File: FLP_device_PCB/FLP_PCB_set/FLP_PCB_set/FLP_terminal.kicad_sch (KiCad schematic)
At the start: 0 parts

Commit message: FLP_set add
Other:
- added sheet BOOT_Mode (BOOT_Mode.kicad_sch)
- added sheet Bat (Bat.kicad_sch)
- added sheet GPS (GPS.kicad_sch)
- added sheet LoRa (LoRa.kicad_sch)
- added sheet USB_to_UART (USB_to_UART.kicad_sch)
- added sheet Voltage_convert (5v_to_3.3V.kicad_sch)
- sheet STM32 ports: added 3.3V_in, BOOT0, BOOT1, DIO0(IRQ), GPS_Reset, GPS_Rx, GPS_TX, MISO, MOSI, NSS(CS), RESET, RX, SCK, TX, VBAT; removed none
- sheet UART_USB ports: added 5V_USB; removed none

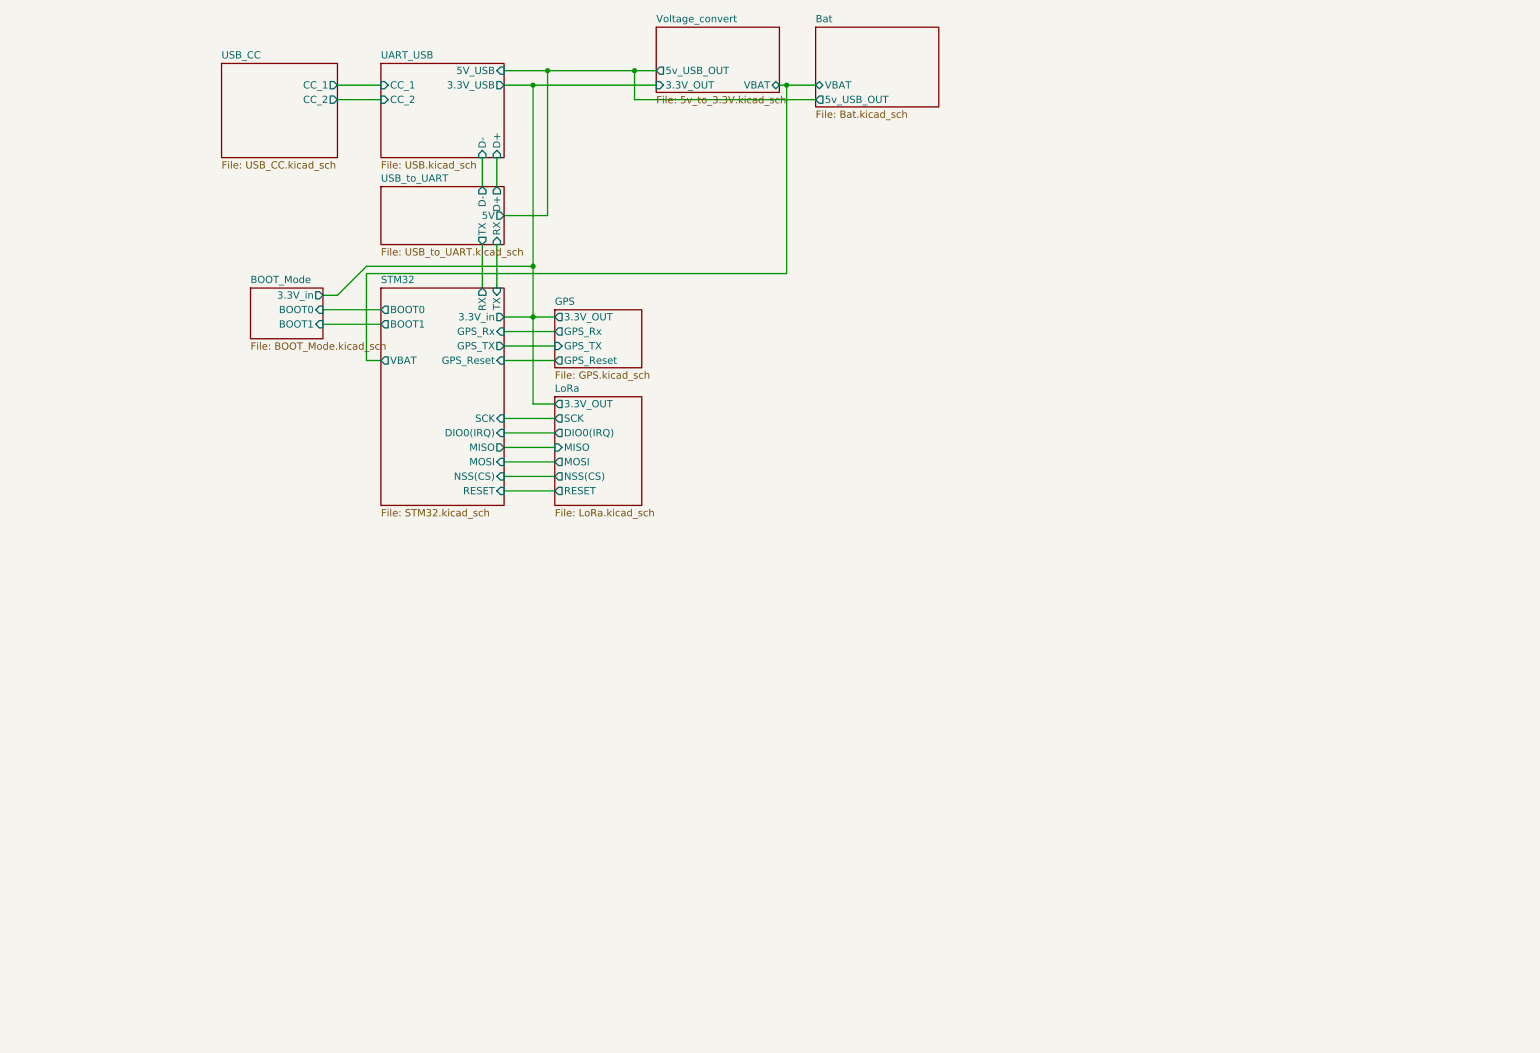
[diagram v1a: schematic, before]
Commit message: PCB fixing end adding description pdf
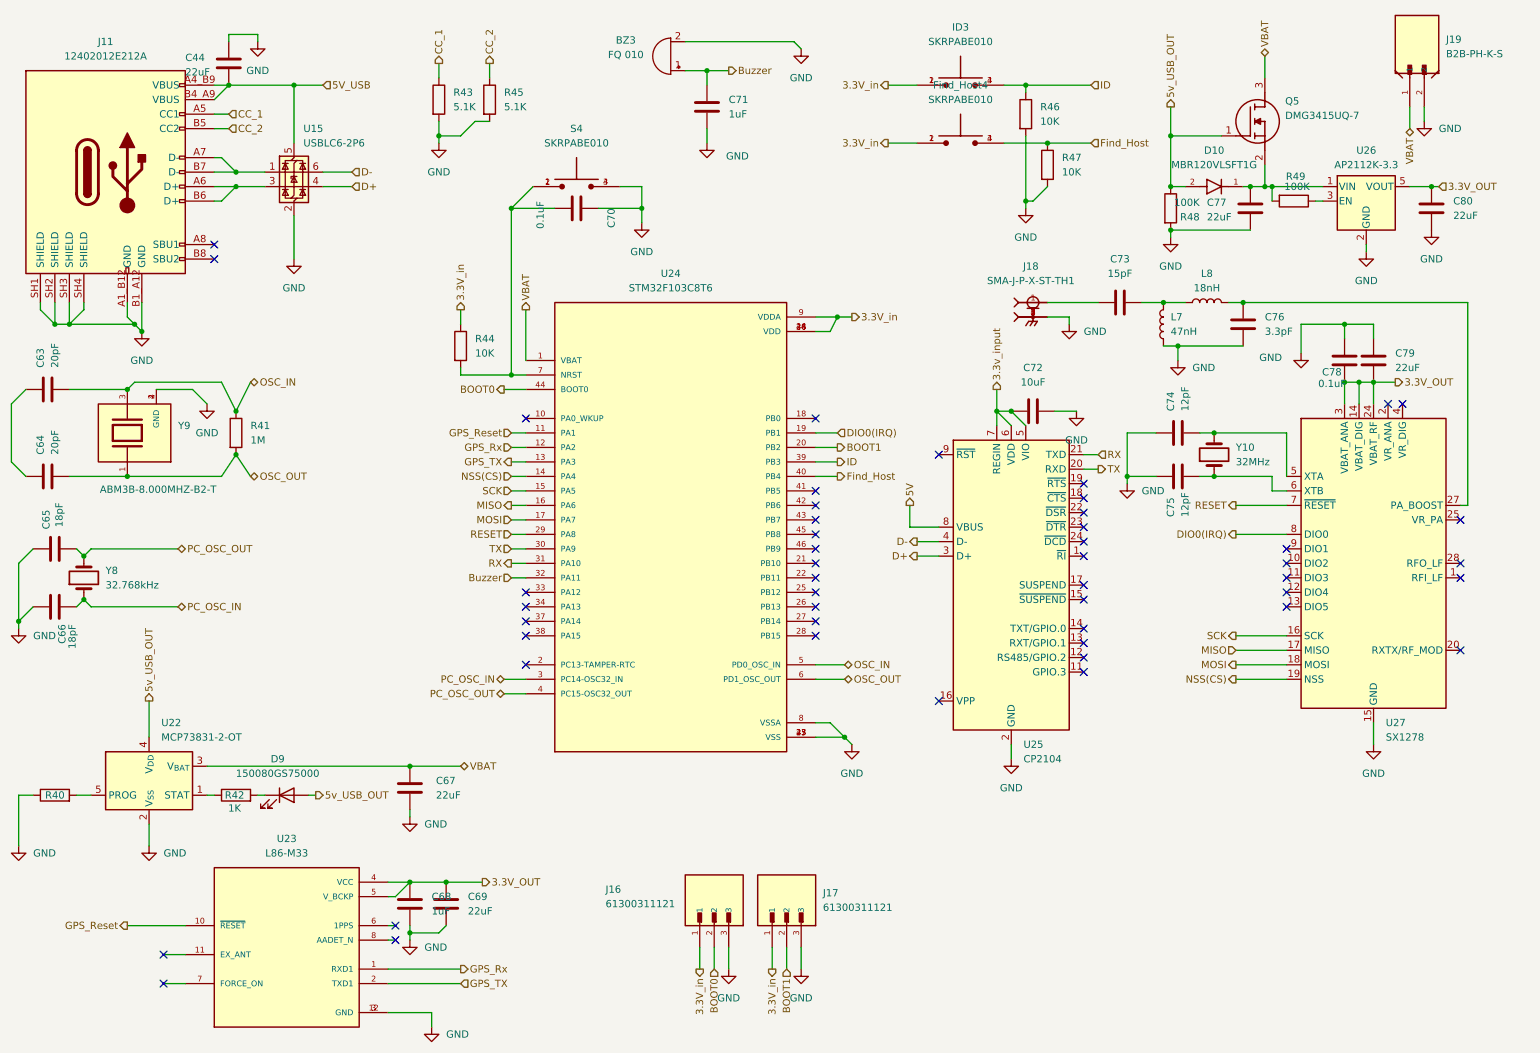
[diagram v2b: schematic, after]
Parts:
- added BZ3: FQ 010, Buzzer_Beeper:Buzzer_12x9.5RM7.6, symbol Device:Buzzer
- added C44, C67, C69, C77, C79, C80: 22uF, Capacitor_SMD:C_0805_2012Metric, symbol Device:C
- added C63, C64: 20pF, Capacitor_SMD:C_0402_1005Metric, symbol Device:C
- added C65, C66: 18pF, Capacitor_SMD:C_0603_1608Metric, symbol Device:C
- added C68, C71: 1uF, Capacitor_SMD:C_0603_1608Metric, symbol Device:C
- added C70, C78: 0.1uF, Capacitor_SMD:C_0603_1608Metric, symbol Device:C
- added C72: 10uF, Capacitor_SMD:C_0805_2012Metric, symbol Device:C
- added C73: 15pF, Capacitor_SMD:C_0402_1005Metric, symbol Device:C
- added C74, C75: 12pF, Capacitor_SMD:C_0402_1005Metric, symbol Device:C
- added C76: 3.3pF, Capacitor_SMD:C_0402_1005Metric, symbol Device:C
- added D10: MBR120VLSFT1G, MBR120VLSFT1G:DIOM3616X98N, symbol MBR120VLSFT1G:MBR120VLSFT1G
- added D9: 150080GS75000, LED_SMD:LED_0805_2012Metric, symbol Device:LED
- added Find_Host4, ID3, S4: SKRPABE010, Diode_SMD:SW_SKRPABE010, symbol SKRPABE010:SKRPABE010
- added J11: 12402012E212A, 12402012E212A:AMPHENOL_12402012E212A, symbol Connector:USB_C_Receptacle_USB2.0_16P
- added J16, J17: 61300311121, 61300311121:WURTH_61300311121, symbol 61300311121:61300311121
- added J18: SMA-J-P-X-ST-TH1, SMA-J-P-X-ST-TH1:SAMTEC_SMA-J-P-X-ST-TH1, symbol SMA-J-P-X-ST-TH1:SMA-J-P-X-ST-TH1
- added J19: B2B-PH-K-S, B2B_PH_K_S:JST_B2B-PH-K-S, symbol B2B-PH-K-S:B2B-PH-K-S
- added L7: 47nH, Inductor_SMD:L_0402_1005Metric, symbol Device:L
- added L8: 18nH, Inductor_SMD:L_0402_1005Metric, symbol Device:L
- added Q5: DMG3415UQ-7, symbol DMG3415UQ-7:DMG3415UQ-7
- added R40: 2K, Resistor_SMD:R_0402_1005Metric, symbol Device:R
- added R41: 1M, Resistor_SMD:R_0603_1608Metric, symbol Device:R
- added R42: 1K, Resistor_SMD:R_0603_1608Metric, symbol Device:R
- added R43, R45: 5.1K, Resistor_SMD:R_0603_1608Metric, symbol Device:R
- added R44, R46, R47: 10K, Resistor_SMD:R_0603_1608Metric, symbol Device:R
- added R48, R49: 100K, Resistor_SMD:R_0603_1608Metric, symbol Device:R
- added U15: USBLC6-2P6, Package_TO_SOT_SMD:SOT-666, symbol Power_Protection:USBLC6-2P6
- added U22: MCP73831-2-OT, Package_TO_SOT_SMD:SOT-23-5, symbol Battery_Management:MCP73831-2-OT
- added U23: L86-M33, L86-M33:XCVR_L86-M33, symbol L86-M33:L86-M33
- added U24: STM32F103C8T6, STM32F103C8T6:QFP50P900X900X160-48N, symbol STM32F103C8T6:STM32F103C8T6
- added U25: CP2104, Package_DFN_QFN:QFN-24-1EP_4x4mm_P0.5mm_EP2.6x2.6mm, symbol Interface_USB:CP2104
- added U26: AP2112K-3.3, Package_TO_SOT_SMD:SOT-23-5, symbol Regulator_Linear:AP2112K-3.3
- added U27: SX1278, Package_DFN_QFN:QFN-28-1EP_6x6mm_P0.65mm_EP4.8x4.8mm, symbol RF:SX1278
- added Y10: 32MHz, Crystal:Crystal_SMD_2016-4Pin_2.0x1.6mm, symbol Device:Crystal
- added Y8: 32.768kHz, Crystal:Crystal_SMD_3215-2Pin_3.2x1.5mm, symbol Device:Crystal
- added Y9: ABM3B-8.000MHZ-B2-T, ABM3B-8.000MHZ-B2-T:XTAL_ABM3B-8.000MHZ-B2-T, symbol ABM3B-8.000MHZ-B2-T:ABM3B-8.000MHZ-B2-T
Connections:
- new net: R40.2, U22.5 (PROG)
- new net: J11.A6 (D+), J11.B6 (D+), U15.3 (I/O2)
- new net: J11.A7 (D-), J11.B7 (D-), U15.1 (I/O1)
- new net: R42.1, U22.1 (STAT)
- new net: C70.2, R44.2, S4.1, S4.2, U24.7 (NRST)
- new net: C63.1, C64.1
- new net: D9.1 (K), R42.2
- new net: C77.1, D10.1, Q5.2 (S), R49.2, U26.1 (VIN)
- new net: R49.1, U26.3 (EN)
- new net: C73.2, J18.1
- new net: C74.2, U27.5 (XTA), Y10.2
- new net: C75.2, U27.6 (XTB), Y10.1
- new net: C76.1, L8.2, U27.27 (PA_BOOST)
- new net: C73.1, L7.2, L8.1
- new net 3.3V_OUT: C68.1, C69.1, C78.1, C79.2, C80.1, U23.4 (VCC), U23.5 (V_BCKP), U26.5 (VOUT), U27.14 (VBAT_DIG), U27.24 (VBAT_RF), U27.3 (VBAT_ANA)
- new net 3.3V_in: Find_Host4.1, Find_Host4.2, ID3.1, ID3.2, J16.1, J17.1, R44.1, U24.24 (VDD), U24.36 (VDD), U24.48 (VDD), U24.9 (VDDA)
- new net 3.3v_input: C72.1, U25.5 (VIO), U25.6 (VDD), U25.7 (REGIN)
- new net 5V: U25.8 (VBUS)
- new net 5V_USB: C44.2, J11.A4_B9 (VBUS), J11.A9 (VBUS), J11.B4 (VBUS), J11.B4_A9 (VBUS), J11.B9 (VBUS), U15.5 (VBUS)
- new net 5v_USB_OUT: D10.2, D9.2 (A), Q5.1 (G), R48.1, U22.4 (V_{DD})
- new net BOOT0: J16.2, U24.44 (BOOT0)
- new net BOOT1: J17.2, U24.20 (PB2)
- new net Buzzer: BZ3.1 (+), C71.1, U24.32 (PA11)
- new net CC_1: J11.A5 (CC1), R43.1
- new net CC_2: J11.B5 (CC2), R45.1
- new net D+: U15.4 (I/O2), U25.3 (D+)
- new net D-: U15.6 (I/O1), U25.4 (D-)
- new net DIO0(IRQ): U24.19 (PB1), U27.8 (DIO0)
- new net Find_Host: Find_Host4.3, Find_Host4.4, R47.1, U24.40 (PB4)
- new net GND: BZ3.2 (-), C44.1, C65.2, C66.2, C67.2, C68.2, C69.2, C70.1, C71.2, C72.2, C74.1, C75.1, C76.2, C77.2, C78.2, C79.1, C80.2, J11.A12 (GND), J11.A1_B12 (GND), J11.B1 (GND), J11.B12 (GND), J11.B1_A12 (GND), J11.SH1 (SHIELD), J11.SH2 (SHIELD), J11.SH3 (SHIELD), J11.SH4 (SHIELD), J16.3, J17.3, J18.2, J18.3, J18.4, J18.5, J19.2, L7.1, R40.1, R43.2, R45.2, R46.2, R47.2, R48.2, S4.3, S4.4, U15.2 (GND), U22.2 (V_{SS}), U23.12 (GND), U23.3 (GND), U24.23 (VSS), U24.35 (VSS), U24.47 (VSS), U24.8 (VSSA), U25.2 (GND), U25.25 (GND), U26.2 (GND), U27.15 (GND), U27.21 (GND), U27.22 (GND), U27.23 (GND), U27.26 (GND), U27.29 (GND), Y9.2 (GND), Y9.4 (GND)
- new net GPS_Reset: U23.10 (~{RESET}), U24.11 (PA1)
- new net GPS_Rx: U23.1 (RXD1), U24.12 (PA2)
- new net GPS_TX: U23.2 (TXD1), U24.13 (PA3)
- new net ID: ID3.3, ID3.4, R46.1, U24.39 (PB3)
- new net MISO: U24.16 (PA6), U27.17 (MISO)
- new net MOSI: U24.17 (PA7), U27.18 (MOSI)
- new net NSS(CS): U24.14 (PA4), U27.19 (NSS)
- new net OSC_IN: C63.2, R41.1, U24.5 (PD0_OSC_IN), Y9.3
- new net OSC_OUT: C64.2, R41.2, U24.6 (PD1_OSC_OUT), Y9.1
- new net PC_OSC_IN: C66.1, U24.3 (PC14-OSC32_IN), Y8.1
- new net PC_OSC_OUT: C65.1, U24.4 (PC15-OSC32_OUT), Y8.2
- new net RESET: U24.29 (PA8), U27.7 (~{RESET})
- new net RX: U24.31 (PA10), U25.21 (TXD)
- new net SCK: U24.15 (PA5), U27.16 (SCK)
- new net TX: U24.30 (PA9), U25.20 (RXD)
- new net VBAT: C67.1, J19.1, Q5.3 (D), U22.3 (V_{BAT}), U24.1 (VBAT)
- no-connect marks 0 -> 49
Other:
- removed sheet BOOT_Mode
- removed sheet Bat
- removed sheet GPS
- removed sheet LoRa
- removed sheet STM32
- removed sheet UART_USB
- removed sheet USB_CC
- removed sheet USB_to_UART
- removed sheet Voltage_convert
